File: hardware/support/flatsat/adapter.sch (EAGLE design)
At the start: 2 parts, among them X1 FH12-40S-0.5SH

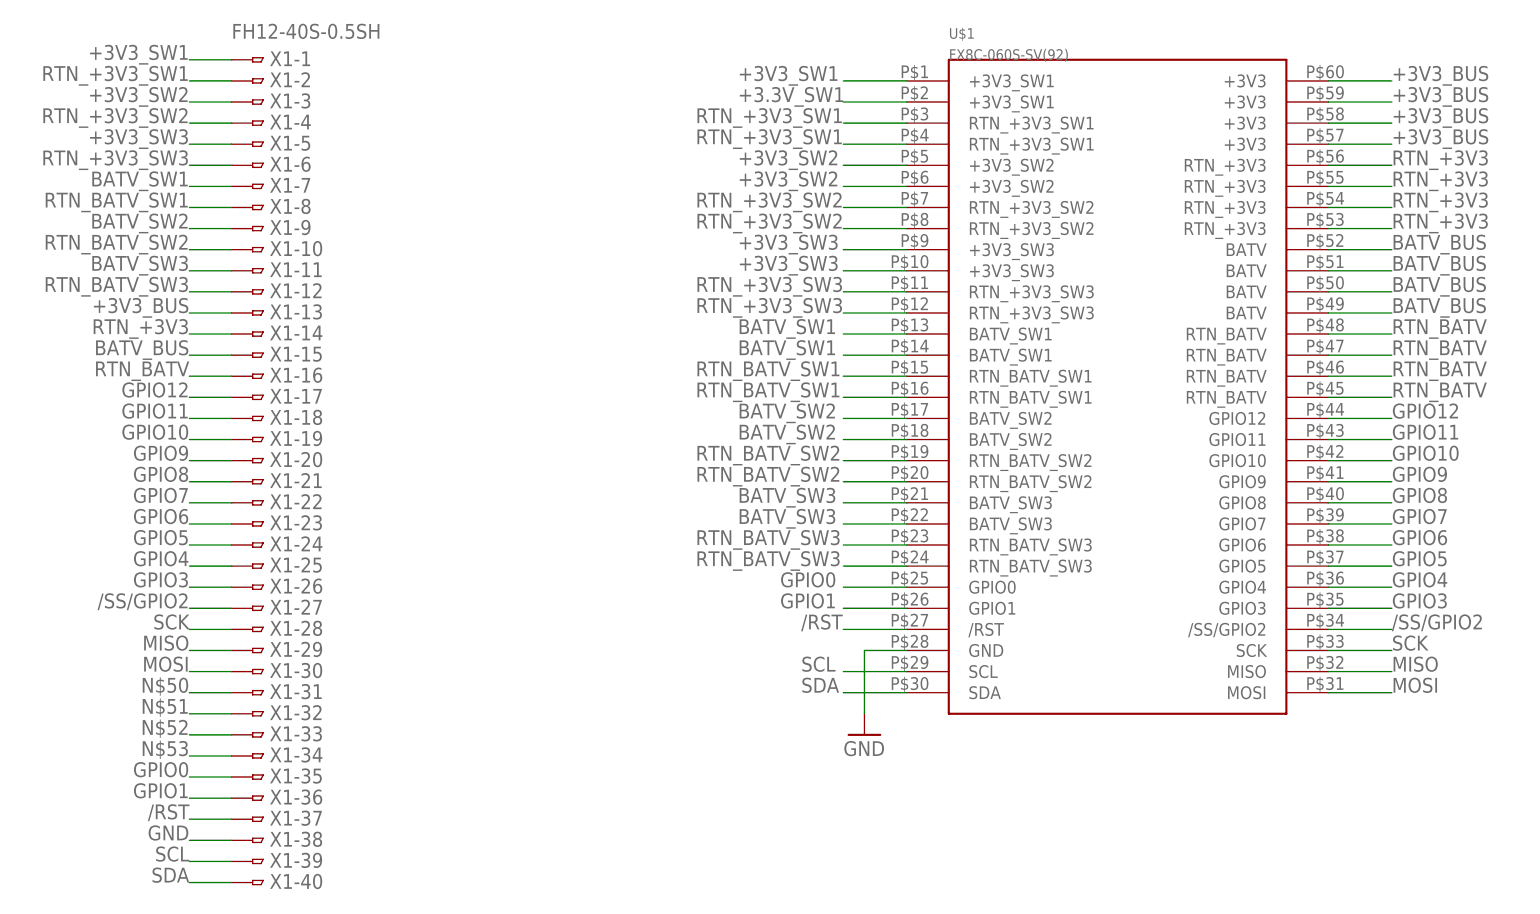
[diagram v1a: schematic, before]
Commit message: added flatsat board and routed
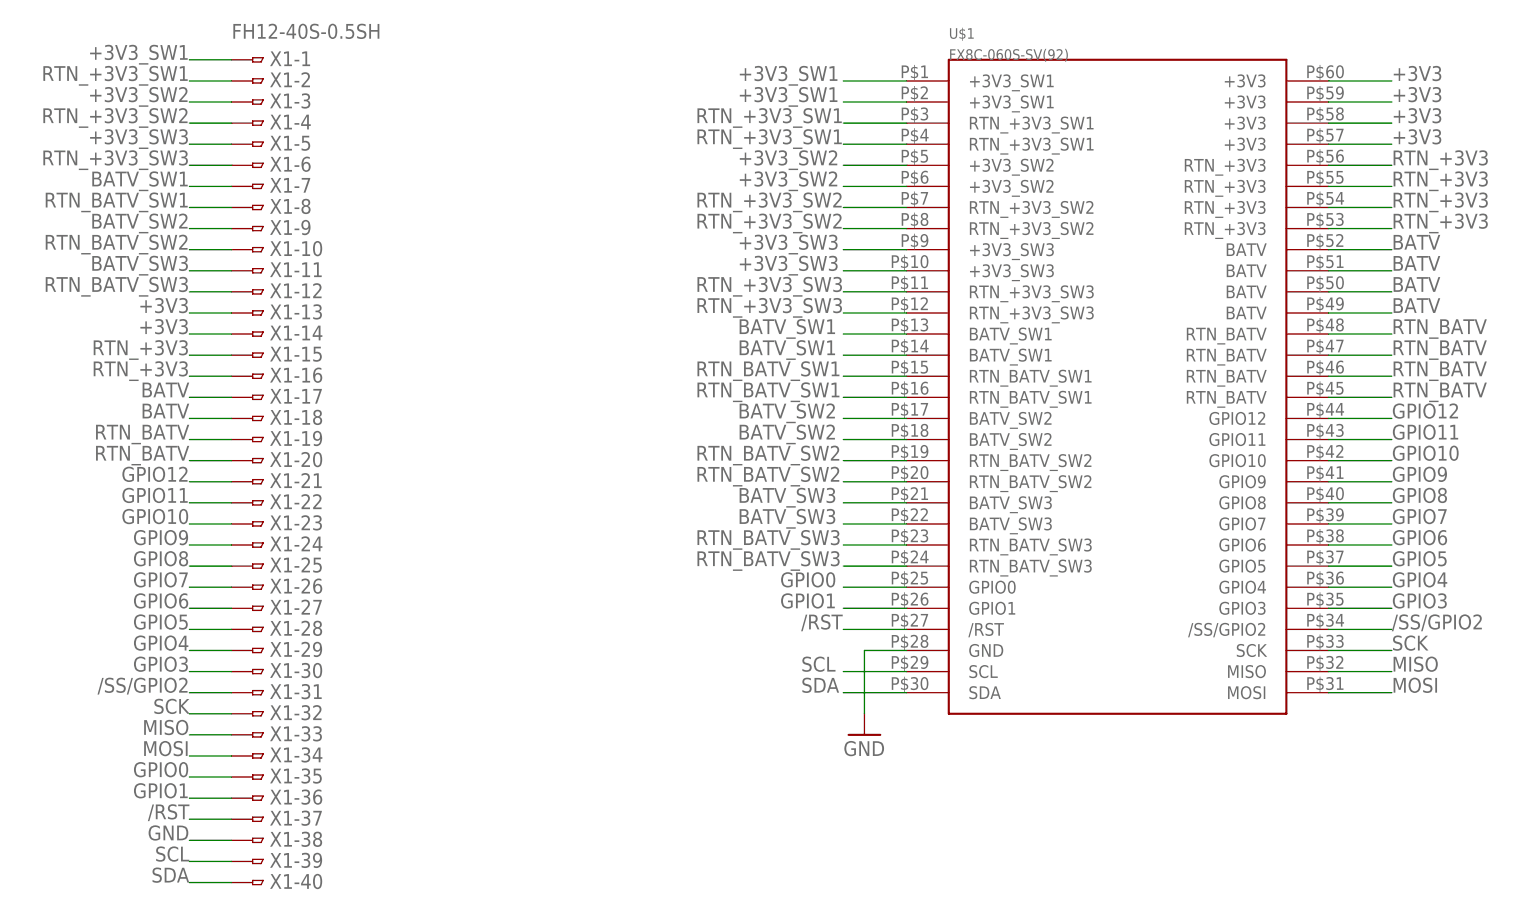
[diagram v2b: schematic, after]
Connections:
- removed net +3.3V_SW1: U$1.+3V3_SW1@2
- removed net +3V3_BUS: U$1.+3V3@1, U$1.+3V3@2, U$1.+3V3@3, U$1.+3V3@4, X1-13.1
- removed net BATV_BUS: U$1.BATV@1, U$1.BATV@2, U$1.BATV@3, U$1.BATV@4, X1-15.1
- removed net N$50: X1-31.1
- removed net N$51: X1-32.1
- removed net N$52: X1-33.1
- removed net N$53: X1-34.1
- new net +3V3: U$1.+3V3@1, U$1.+3V3@2, U$1.+3V3@3, U$1.+3V3@4, X1-13.1, X1-14.1
- new net BATV: U$1.BATV@1, U$1.BATV@2, U$1.BATV@3, U$1.BATV@4, X1-17.1, X1-18.1
- net +3V3_SW1: now also U$1.+3V3_SW1@2
- net /SS/GPIO2: now also X1-31.1; no longer X1-27.1
- net GPIO10: now also X1-23.1; no longer X1-19.1
- net GPIO11: now also X1-22.1; no longer X1-18.1
- net GPIO12: now also X1-21.1; no longer X1-17.1
- net GPIO3: now also X1-30.1; no longer X1-26.1
- net GPIO4: now also X1-29.1; no longer X1-25.1
- net GPIO5: now also X1-28.1; no longer X1-24.1
- net GPIO6: now also X1-27.1; no longer X1-23.1
- net GPIO7: now also X1-26.1; no longer X1-22.1
- net GPIO8: now also X1-25.1; no longer X1-21.1
- net GPIO9: now also X1-24.1; no longer X1-20.1
- net MISO: now also X1-33.1; no longer X1-29.1
- net MOSI: now also X1-34.1; no longer X1-30.1
- net RTN_+3V3: now also X1-15.1, X1-16.1; no longer X1-14.1
- net RTN_BATV: now also X1-19.1, X1-20.1; no longer X1-16.1
- net SCK: now also X1-32.1; no longer X1-28.1
